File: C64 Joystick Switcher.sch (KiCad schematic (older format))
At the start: 31 parts, among them J1 Port 1, J2 Port 2, J3 Mega Drive, J4 B2_SEL, J5 B1_SEL, Q1 BC547, SW1 P1_SEL, SW2 P2_SEL, U1 74HCT4053, U2 74HCT4053, U3 NE555, U4 NE555

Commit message: Gerber export
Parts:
- J3: value Mega Drive -> Joystick; symbol master_joypad -> Atari_Joystick
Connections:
- net VCC: no longer J3.5 (VCC)
- no-connect marks 5 -> 6
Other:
- note added: "A"
- note added: "Did the Mega Switcher for the Commodore 64 and that works, so the next step was a\nnormal joystick switcher with and autofire inspired from one of MsMadLemons videos. If\nyou do not have a secondary fire button, you can opt to hardwire B1/B2 and not install\nthe circuit for it."
- note added: "Optional ALT_FIRE"
- moved on the sheet: Q1, R5, R6, R7

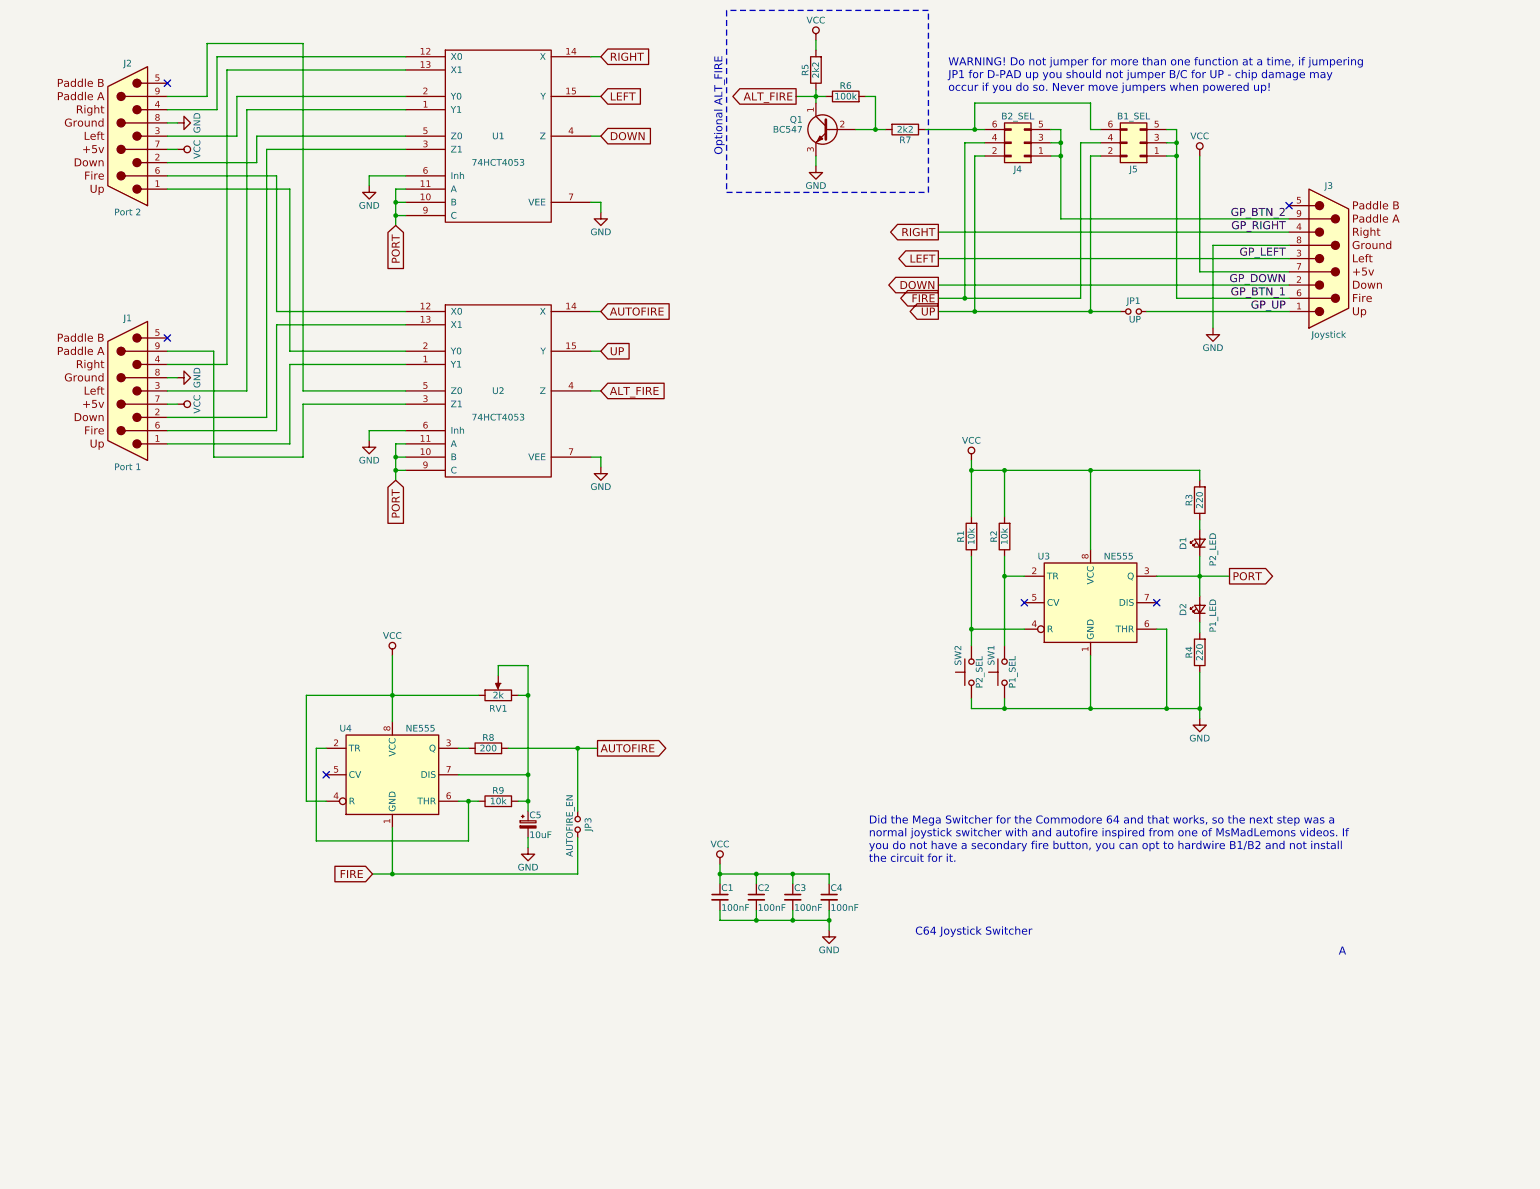
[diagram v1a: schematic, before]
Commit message: Replace auto-fire circuit
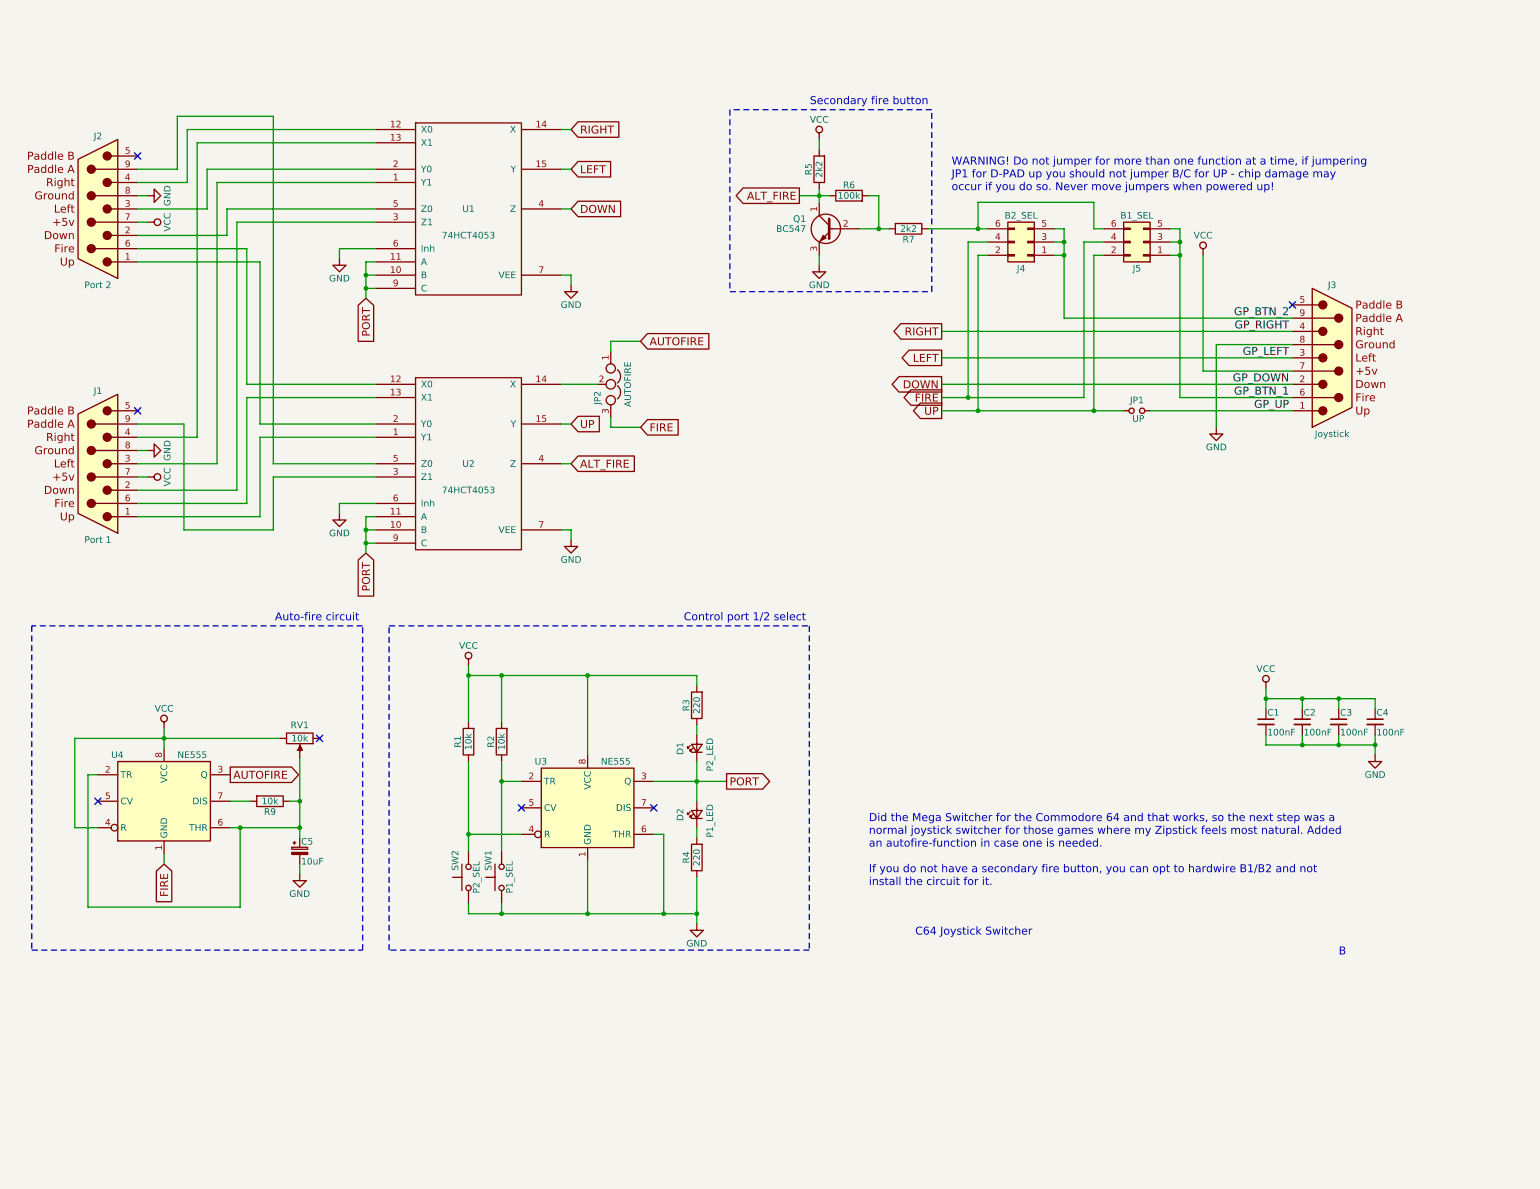
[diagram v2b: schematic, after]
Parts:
- removed JP3: AUTOFIRE_EN, Pin_Headers:Pin_Header_Straight_1x02_Pitch2.54mm, symbol Jumper_NO_Small
- removed R8: 200, Resistors_THT:R_Axial_DIN0207_L6.3mm_D2.5mm_P10.16mm_Horizontal, symbol R
- added JP2: AUTOFIRE, Pin_Headers:Pin_Header_Straight_1x03_Pitch2.54mm, symbol Jumper_NC_Dual
- RV1: value 2k -> 10k
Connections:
- net AUTOFIRE: now also U4.3 (Q), JP2.1; no longer U2.14 (X)
- net FIRE: now also JP2.3
- net VCC: now also RV1.3; no longer RV1.1
- net at R9.1, U4.2 (TR), U4.6 (THR): now also C5.1, RV1.2
- new net: JP2.2, U2.14 (X)
- new net: R9.2, U4.7 (DIS)
- no-connect marks 6 -> 7
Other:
- note added: "Auto-fire circuit"
- note added: "B"
- note added: "Control port 1/2 select"
- note added: "Did the Mega Switcher for the Commodore 64 and that works, so the next step was a\nnormal joystick switcher for those games where my Zipstick feels most natural. Added\nan autofire-function in case one is needed.\n\nIf you do not have a secondary fire button, you can opt to hardwire B1/B2 and not\ninstall the circuit for it."
- note added: "Secondary fire button"
- note removed: "A"
- note removed: "Did the Mega Switcher for the Commodore 64 and that works, so the next step was a\nnormal joystick switcher with and autofire inspired from one of MsMadLemons videos. If\nyou do not have a secondary fire button, you can opt to hardwire B1/B2 and not install\nthe circuit for it."
- note removed: "Optional ALT_FIRE"
- moved on the sheet: C1, C2, C3, C4, C5, D1, D2, J1, J2, J3, J4, J5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

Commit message: Auto-fire should now work
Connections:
- net at C5.1, R9.1, U4.2 (TR)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: no longer RV1.2
- net at R9.2, U4.7 (DIS): now also RV1.2
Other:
- moved on the sheet: C5, R9
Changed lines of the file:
@@
 L R R9
 U 1 1 5D8CCFE2
-P 2475 6475
-F 0 "R9" V 2555 6475 50  0000 C CNN
-F 1 "10k" V 2475 6475 50  0000 C CNN
-F 2 "Resistors_THT:R_Axial_DIN0207_L6.3mm_D2.5mm_P10.16mm_Horizontal" V 2405 6475 50  0001 C CNN
-F 3 "" H 2475 6475 50  0001 C CNN
-	1    2475 6475
-	0    1    1    0
+P 2700 6700
+F 0 "R9" V 2780 6700 50  0000 C CNN
+F 1 "10k" V 2700 6700 50  0000 C CNN
+F 2 "Resistors_THT:R_Axial_DIN0207_L6.3mm_D2.5mm_P10.16mm_Horizontal" V 2630 6700 50  0001 C CNN
+F 3 "" H 2700 6700 50  0001 C CNN
+	1    2700 6700
+	-1   0    0    1
 $EndComp
 $Comp
 L CP_Small C5
 U 1 1 5D8CD3EA
-P 2700 6850
-F 0 "C5" H 2710 6920 50  0000 L CNN
-F 1 "10uF" H 2710 6770 50  0000 L CNN
-F 2 "Capacitors_THT:CP_Radial_D5.0mm_P2.50mm" H 2700 6850 50  0001 C CNN
-F 3 "" H 2700 6850 50  0001 C CNN
-	1    2700 6850
+P 2700 7075
+F 0 "C5" H 2710 7145 50  0000 L CNN
+F 1 "10uF" H 2710 6995 50  0000 L CNN
+F 2 "Capacitors_THT:CP_Radial_D5.0mm_P2.50mm" H 2700 7075 50  0001 C CNN
+F 3 "" H 2700 7075 50  0001 C CNN
+	1    2700 7075
 	1    0    0    -1
 $EndComp
@@
 L GND #PWR017
 U 1 1 5D8CF604
-P 2700 7025
-F 0 "#PWR017" H 2700 6775 50  0001 C CNN
-F 1 "GND" H 2700 6875 50  0000 C CNN
-F 2 "" H 2700 7025 50  0001 C CNN
-F 3 "" H 2700 7025 50  0001 C CNN
-	1    2700 7025
+P 2700 7250
+F 0 "#PWR017" H 2700 7000 50  0001 C CNN
+F 1 "GND" H 2700 7100 50  0000 C CNN
+F 2 "" H 2700 7250 50  0001 C CNN
+F 3 "" H 2700 7250 50  0001 C CNN
+	1    2700 7250
 	1    0    0    -1
 $EndComp
@@
 	2250 7275 2250 6675
 Wire Wire Line
-	2700 6675 2175 6675
+	2250 6675 2175 6675
 Wire Wire Line
 	1675 5925 1675 6075
@@
 Connection ~ 1675 6000
 Wire Wire Line
-	2175 6475 2325 6475
-Wire Wire Line
-	2700 6150 2700 6750
-Connection ~ 2250 6675
-Wire Wire Line
-	2700 6475 2625 6475
-Connection ~ 2700 6675
+	2175 6475 2700 6475
+Wire Wire Line
+	2700 6150 2700 6550
 Connection ~ 2700 6475
 Wire Wire Line
-	2700 7025 2700 6950
+	2700 7250 2700 7175
 Wire Wire Line
 	5275 3000 5050 3000
@@
 Text Notes 7450 1225 2    60   ~ 0
 Secondary fire button
+Wire Wire Line
+	2700 6850 2700 6975
+Wire Wire Line
+	2700 6900 2250 6900
+Connection ~ 2250 6900
+Connection ~ 2700 6900
 $EndSCHEMATC
